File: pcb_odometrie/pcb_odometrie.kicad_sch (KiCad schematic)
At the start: 2 parts, among them J1 1755736, U1 STM32G491KEU6

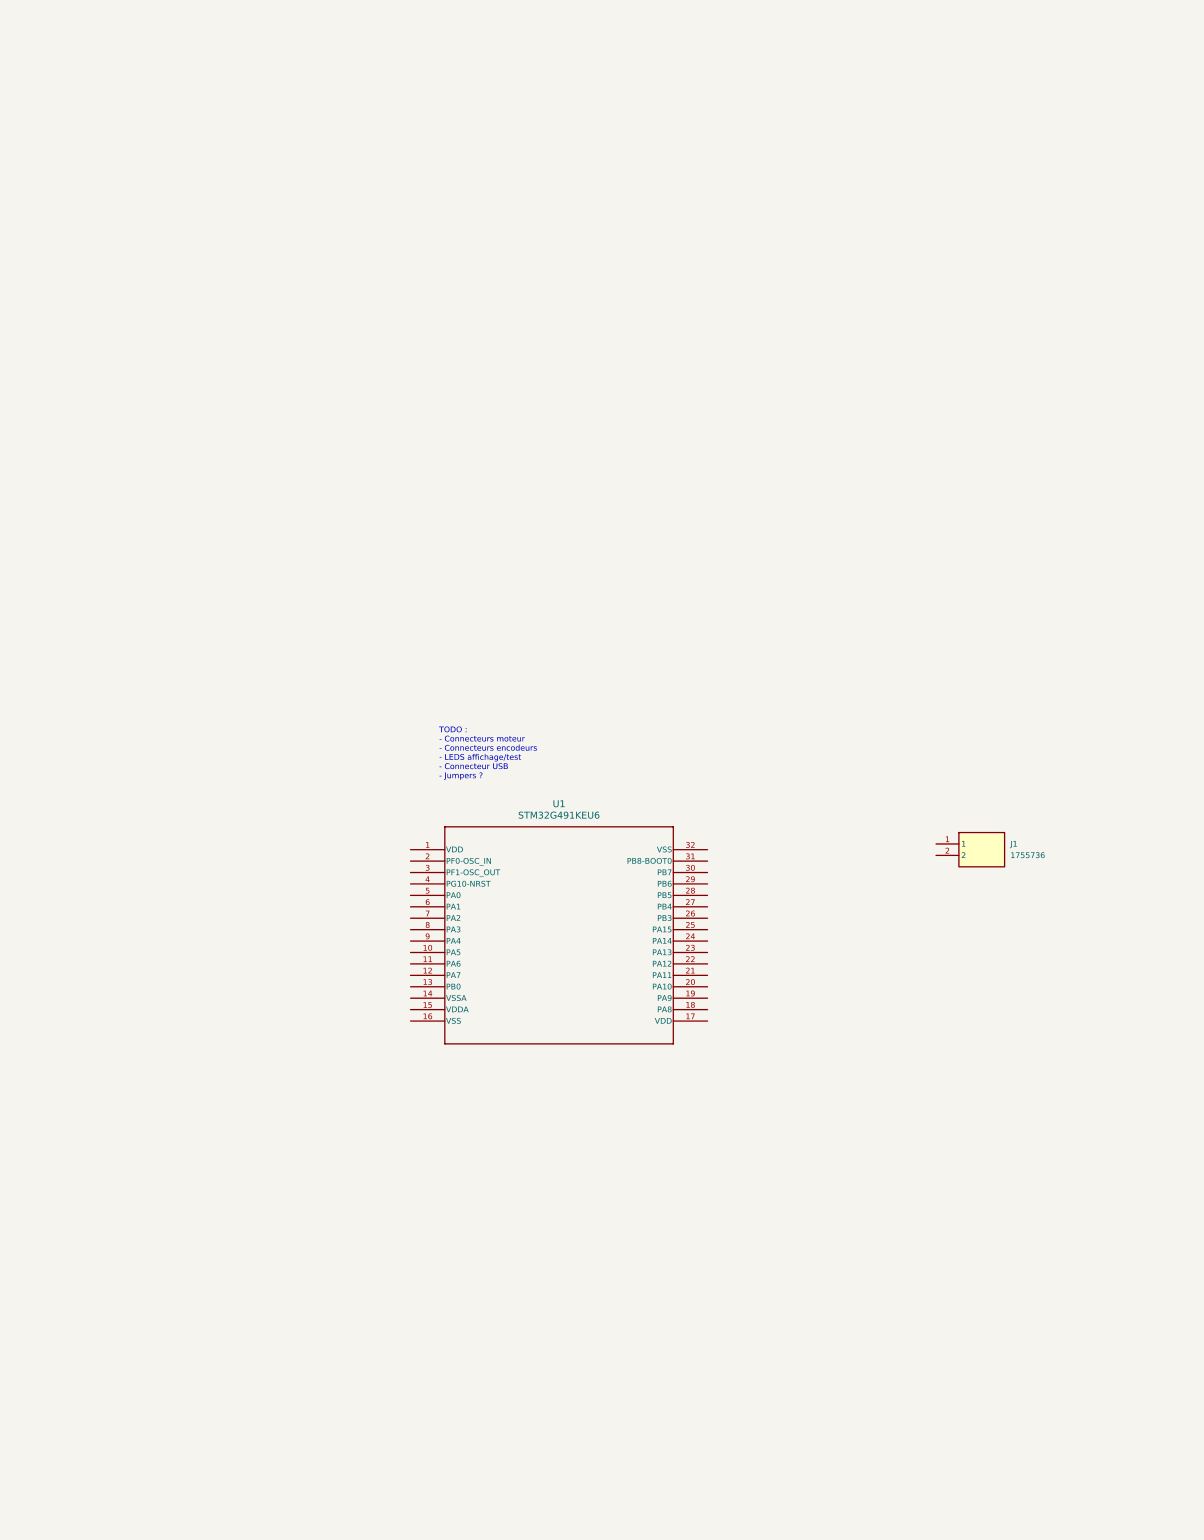
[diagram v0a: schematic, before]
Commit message: correction alim PAMI et travail odo (WIP)
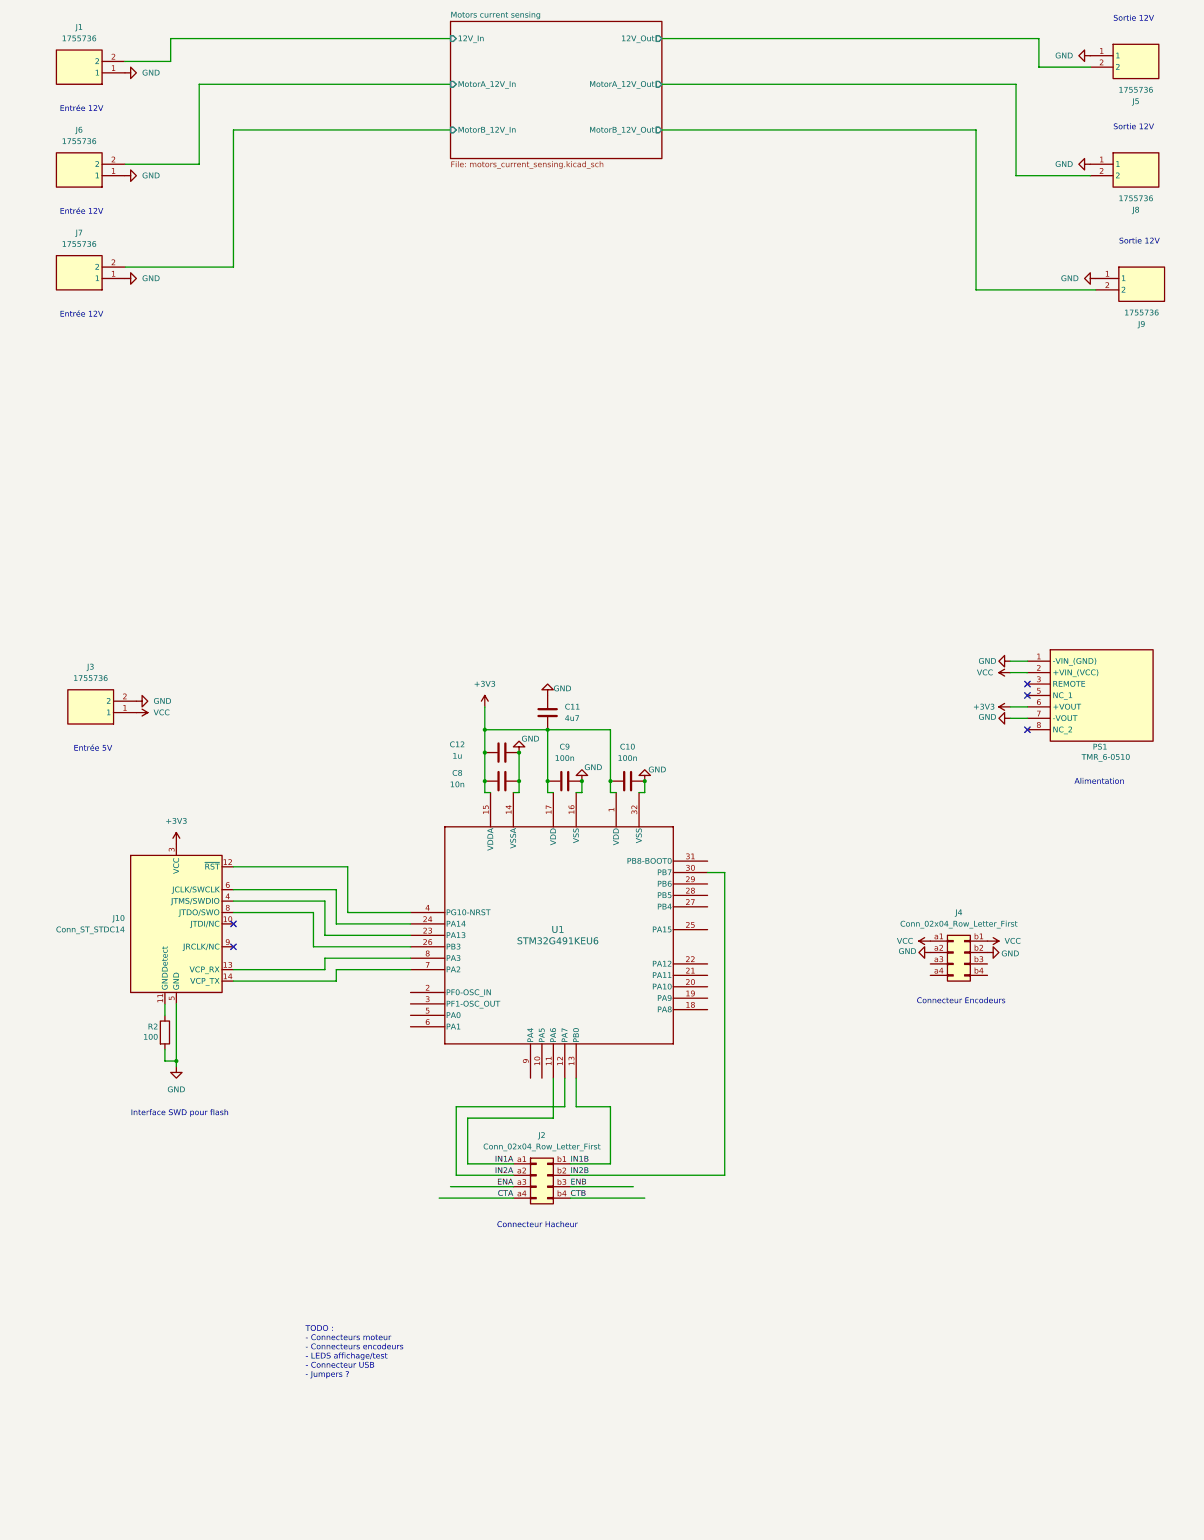
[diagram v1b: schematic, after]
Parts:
- added C10, C9: 100n, Capacitor_SMD:C_0805_2012Metric_Pad1.18x1.45mm_HandSolder, symbol Device:C
- added C11: 4u7, Capacitor_SMD:C_0805_2012Metric_Pad1.18x1.45mm_HandSolder, symbol Device:C
- added C12: 1u, Capacitor_SMD:C_0805_2012Metric_Pad1.18x1.45mm_HandSolder, symbol Device:C
- added C8: 10n, Capacitor_SMD:C_0805_2012Metric_Pad1.18x1.45mm_HandSolder, symbol Device:C
- added J10: Conn_ST_STDC14, Connector_PinHeader_1.27mm:PinHeader_2x07_P1.27mm_Vertical, symbol Connector:Conn_ST_STDC14
- added J2, J4: Conn_02x04_Row_Letter_First, symbol Connector_Generic:Conn_02x04_Row_Letter_First
- added J3, J5, J6, J7, J8, J9: 1755736, 1755736, symbol Modelec:1755736
- added PS1: TMR_6-0510, TMR60510, symbol Modelec:TMR_6-0510
- added R2: 100, Resistor_SMD:R_0805_2012Metric_Pad1.20x1.40mm_HandSolder, symbol Device:R
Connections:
- net GND: now reaches J1.1
- net GND: now also U1.14 (VSSA), U1.16 (VSS), U1.32 (VSS), C10.2, C11.2, C12.2, C8.2, C9.2, J10.5 (GND), J10.7 (GND), J3.2, J4.a2 (Pin_a2), J4.b2 (Pin_b2), J5.1, J6.1, J7.1, J8.1, J9.1, PS1.1 (-VIN_(GND)), PS1.7 (-VOUT), R2.2
- net Motors current sensing/12V_In: now reaches J1.2
- net +3V3: now reaches U1.1 (VDD)
- net +3V3: now also U1.15 (VDDA), U1.17 (VDD), C10.1, C11.1, C12.1, C8.1, C9.1, J10.3 (VCC), PS1.6 (+VOUT)
- net IN1A: now reaches U1.11 (PA6)
- net IN1A: now also J2.a1 (Pin_a1)
- net IN2A: now reaches U1.12 (PA7)
- net IN2A: now also J2.a2 (Pin_a2)
- net IN1B: now reaches U1.13 (PB0)
- net IN1B: now also J2.b1 (Pin_b1)
- net at U1.23 (PA13): now also J10.4 (JTMS/SWDIO)
- net at U1.24 (PA14): now also J10.6 (JCLK/SWCLK)
- net at U1.26 (PB3): now also J10.8 (JTDO/SWO)
- net IN2B: now reaches U1.30 (PB7)
- net IN2B: now also J2.b2 (Pin_b2)
- net at U1.4 (PG10-NRST): now also J10.12 (~{RST})
- net at U1.7 (PA2): now also J10.14 (VCP_TX)
- net at U1.8 (PA3): now also J10.13 (VCP_RX)
- new net: J10.11 (GNDDetect), R2.1
- new net CTA: J2.a4 (Pin_a4)
- new net CTB: J2.b4 (Pin_b4)
- new net ENA: J2.a3 (Pin_a3)
- new net ENB: J2.b3 (Pin_b3)
- new net Motors current sensing/12V_Out: J5.2
- new net Motors current sensing/MotorA_12V_In: J6.2
- new net Motors current sensing/MotorA_12V_Out: J8.2
- new net Motors current sensing/MotorB_12V_In: J7.2
- new net Motors current sensing/MotorB_12V_Out: J9.2
- new net VCC: J3.1, J4.a1 (Pin_a1), J4.b1 (Pin_b1), PS1.2 (+VIN_(VCC))
- no-connect marks 0 -> 5
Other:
- added sheet Motors current sensing (motors_current_sensing.kicad_sch)
- note added: "Alimentation"
- note added: "Connecteur Encodeurs"
- note added: "Connecteur Hacheur"
- note added: "Entrée 12V"
- note added: "Entrée 5V"
- note added: "Interface SWD pour flash"
- note added: "Sortie 12V"
- moved on the sheet: J1

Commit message: PCB odometrie schema fini
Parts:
- removed J1, J5, J6, J7, J8, J9: 1755736, 1755736, symbol Modelec:1755736
- added J1: USB_C_Receptacle_USB2.0_16P, symbol Connector:USB_C_Receptacle_USB2.0_16P
- added R2, R3: 5K1, symbol Device:R
- added R4: 10k, Resistor_SMD:R_0805_2012Metric_Pad1.20x1.40mm_HandSolder, symbol Device:R
- renumbered C12 to C1, C8 to C2, C11 to C3, C9 to C4, C10 to C5, J10 to J2, J2 to J4, J4 to J5, R2 to R1
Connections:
- net CTA: now also U1.12 (PA7)
- net CTB: now also U1.11 (PA6)
- net ENA: now also U1.20 (PA10)
- net ENB: now also U1.13 (PB0)
- net GND: now also J1.A1 (GND), J1.A12 (GND), J1.B1 (GND), J1.B12 (GND), J1.S1 (SHIELD), R2.2, R3.2, R4.1
- net IN1A: now also U1.18 (PA8); no longer U1.11 (PA6)
- net IN1B: now also U1.29 (PB6); no longer U1.13 (PB0)
- net IN2A: now also U1.19 (PA9); no longer U1.12 (PA7)
- net IN2B: now also U1.31 (PB8-BOOT0), R4.2; no longer U1.30 (PB7)
- net at U1.10 (PA5): now also J5.a3 (Pin_a3)
- net USB_DM: now reaches U1.21 (PA11)
- net USB_DM: now also J1.A7 (D-), J1.B7 (D-)
- net USB_DP: now reaches U1.22 (PA12)
- net USB_DP: now also J1.A6 (D+), J1.B6 (D+)
- net I2C1_SCL: now reaches U1.25 (PA15)
- net EVENTOUTB: now reaches U1.27 (PB4)
- net EVENTOUTA: now reaches U1.28 (PB5)
- net at U1.5 (PA0): now also J5.b3 (Pin_b3)
- net at U1.6 (PA1): now also J5.b4 (Pin_b4)
- net at U1.9 (PA4): now also J5.a4 (Pin_a4)
- new net: J1.B5 (CC2), R3.1
- new net: J1.A5 (CC1), R2.1
- new net: J1.A4 (VBUS), J1.A9 (VBUS), J1.B4 (VBUS), J1.B9 (VBUS)
- new net I2C1_SDA: U1.30 (PB7)
- no-connect marks 5 -> 10
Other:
- removed sheet Motors current sensing
- added sheet ToF connectors (tof.kicad_sch)
- note added: "TODO : - LEDS affichage/test - Jumpers ?"
- note removed: "Entrée 12V"
- note removed: "Sortie 12V"
- note removed: "TODO : - Connecteurs moteur - Connecteurs encodeurs - LEDS affichage/test - Connecteur USB - Jumpers ?"
- moved on the sheet: C1, C2, C3, C4, C5, J2, J3, J4, J5, PS1, R1, U1

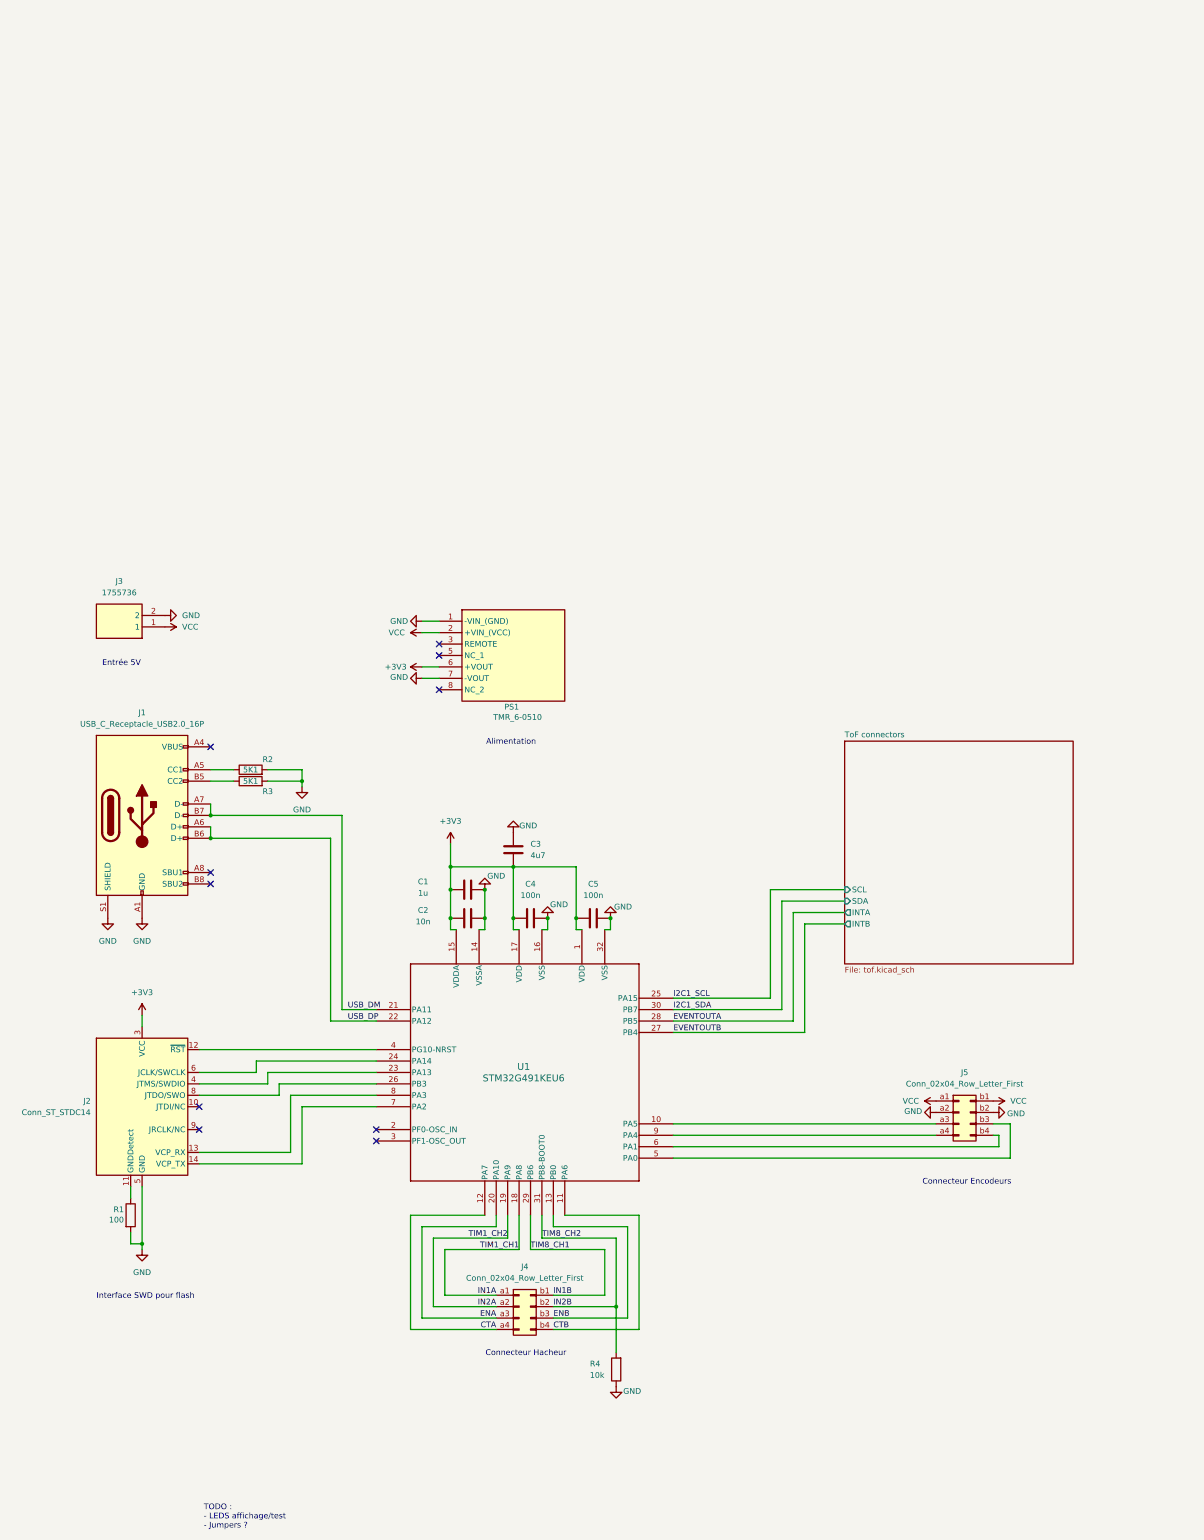
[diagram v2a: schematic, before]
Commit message: routage pcb odométrie fait : reste quelques reglages pour s'adapter au DBH-12
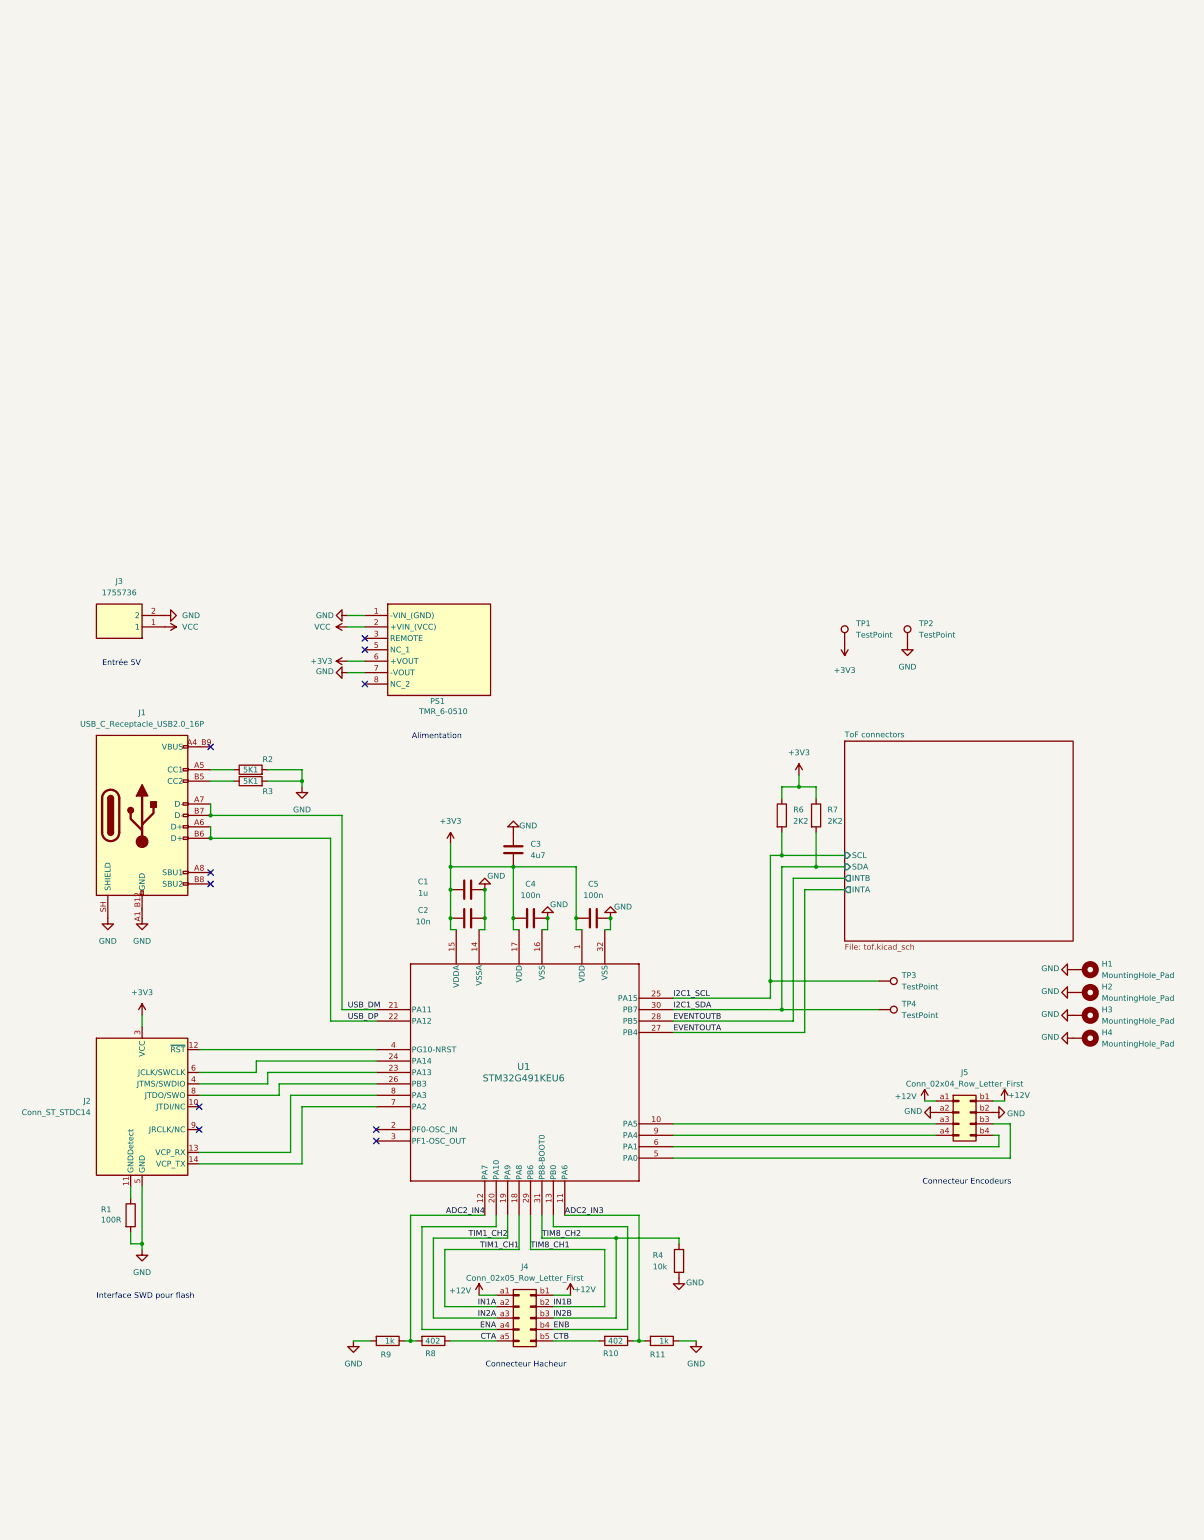
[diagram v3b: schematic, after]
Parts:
- removed J4: Conn_02x04_Row_Letter_First, symbol Connector_Generic:Conn_02x04_Row_Letter_First
- added H1, H2, H3, H4: MountingHole_Pad, MountingHole:MountingHole_3.2mm_M3_ISO14580_Pad_TopBottom, symbol Mechanical:MountingHole_Pad
- added J4: Conn_02x05_Row_Letter_First, Connector_PinSocket_1.27mm:PinSocket_2x05_P1.27mm_Vertical, symbol Connector_Generic:Conn_02x05_Row_Letter_First
- added R10, R8: 402, Resistor_SMD:R_0805_2012Metric_Pad1.20x1.40mm_HandSolder, symbol Device:R
- added R11, R9: 1k, Resistor_SMD:R_0805_2012Metric_Pad1.20x1.40mm_HandSolder, symbol Device:R
- added R6, R7: 2K2, Resistor_SMD:R_0805_2012Metric_Pad1.20x1.40mm_HandSolder, symbol Device:R
- added TP1, TP2, TP3, TP4: TestPoint, TestPoint:TestPoint_Bridge_Pitch2.54mm_Drill0.7mm, symbol Connector:TestPoint
- J1: footprint (none) -> Modelec:GCT_USB4105-GF-A
- J3: footprint 1755736 -> Modelec:PhoenixContact_MSTBVA_2,5_2-G-5,08_1x02_P5.08mm_Vertical
- J5: footprint (none) -> Connector_PinHeader_1.27mm:PinHeader_2x04_P1.27mm_Vertical
- PS1: footprint TMR60510 -> Modelec:TMR60510
- R1: value 100 -> 100R
- R2, R3: footprint (none) -> Resistor_SMD:R_0805_2012Metric_Pad1.20x1.40mm_HandSolder
- U1: footprint UFQFPN32_STM -> Modelec:STM32G491KEU6
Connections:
- net +3V3: now also R6.1, R7.1, TP1.1
- net CTA: now also J4.a5 (Pin_a5), R8.1; no longer U1.12 (PA7)
- net CTB: now also J4.b5 (Pin_b5), R10.2; no longer U1.11 (PA6)
- net ENA: now also J4.a4 (Pin_a4)
- net ENB: now also J4.b4 (Pin_b4)
- net EVENTOUTA: now also U1.27 (PB4); no longer U1.28 (PB5)
- net EVENTOUTB: now also U1.28 (PB5); no longer U1.27 (PB4)
- net GND: now also J1.A1_B12 (GND), J1.B1_A12 (GND), J1.SH (SHIELD), H1.1, H2.1, H3.1, H4.1, R11.1, R9.2, TP2.1; no longer J1.A1 (GND), J1.A12 (GND), J1.B1 (GND), J1.B12 (GND), J1.S1 (SHIELD)
- net I2C1_SCL: now also R6.2, TP3.1
- net I2C1_SDA: now also R7.2, TP4.1
- net IN1A: now also J4.a2 (Pin_a2)
- net IN1B: now also J4.b2 (Pin_b2)
- net IN2A: now also J4.a3 (Pin_a3)
- net IN2B: now also J4.b3 (Pin_b3)
- net VCC: no longer J5.a1 (Pin_a1), J5.b1 (Pin_b1)
- new net: J1.A4_B9 (VBUS), J1.B4_A9 (VBUS)
- new net +12V: J4.a1 (Pin_a1), J4.b1 (Pin_b1), J5.a1 (Pin_a1), J5.b1 (Pin_b1)
- new net ADC2_IN3: R10.1, R11.2, U1.11 (PA6)
- new net ADC2_IN4: R8.2, R9.1, U1.12 (PA7)
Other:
- note removed: "TODO : - LEDS affichage/test - Jumpers ?"
- moved on the sheet: J1, PS1, R4
